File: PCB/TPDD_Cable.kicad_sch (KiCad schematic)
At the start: 9 parts, among them J1 TPDD_RS-232C, P3 RX, P4 RTS, P5 CTS, P6 DSR, Q1 DTA114EKA, Q2 DTA114EKA, Q3 DTA114EKA

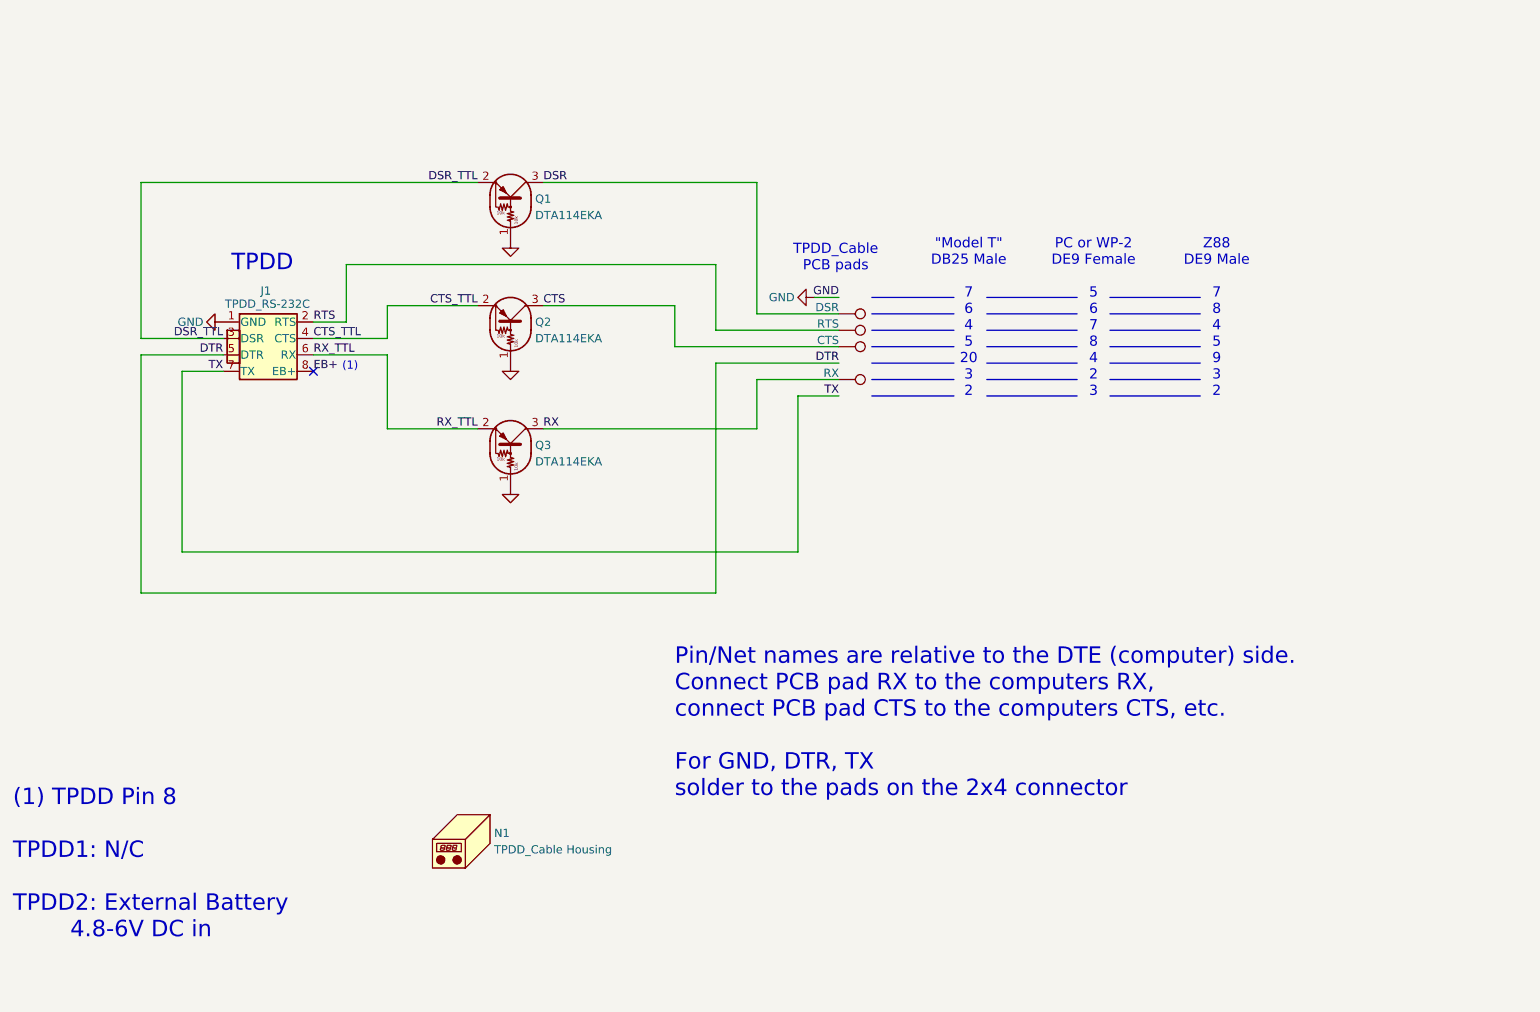
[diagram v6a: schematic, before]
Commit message: schematic less clutter
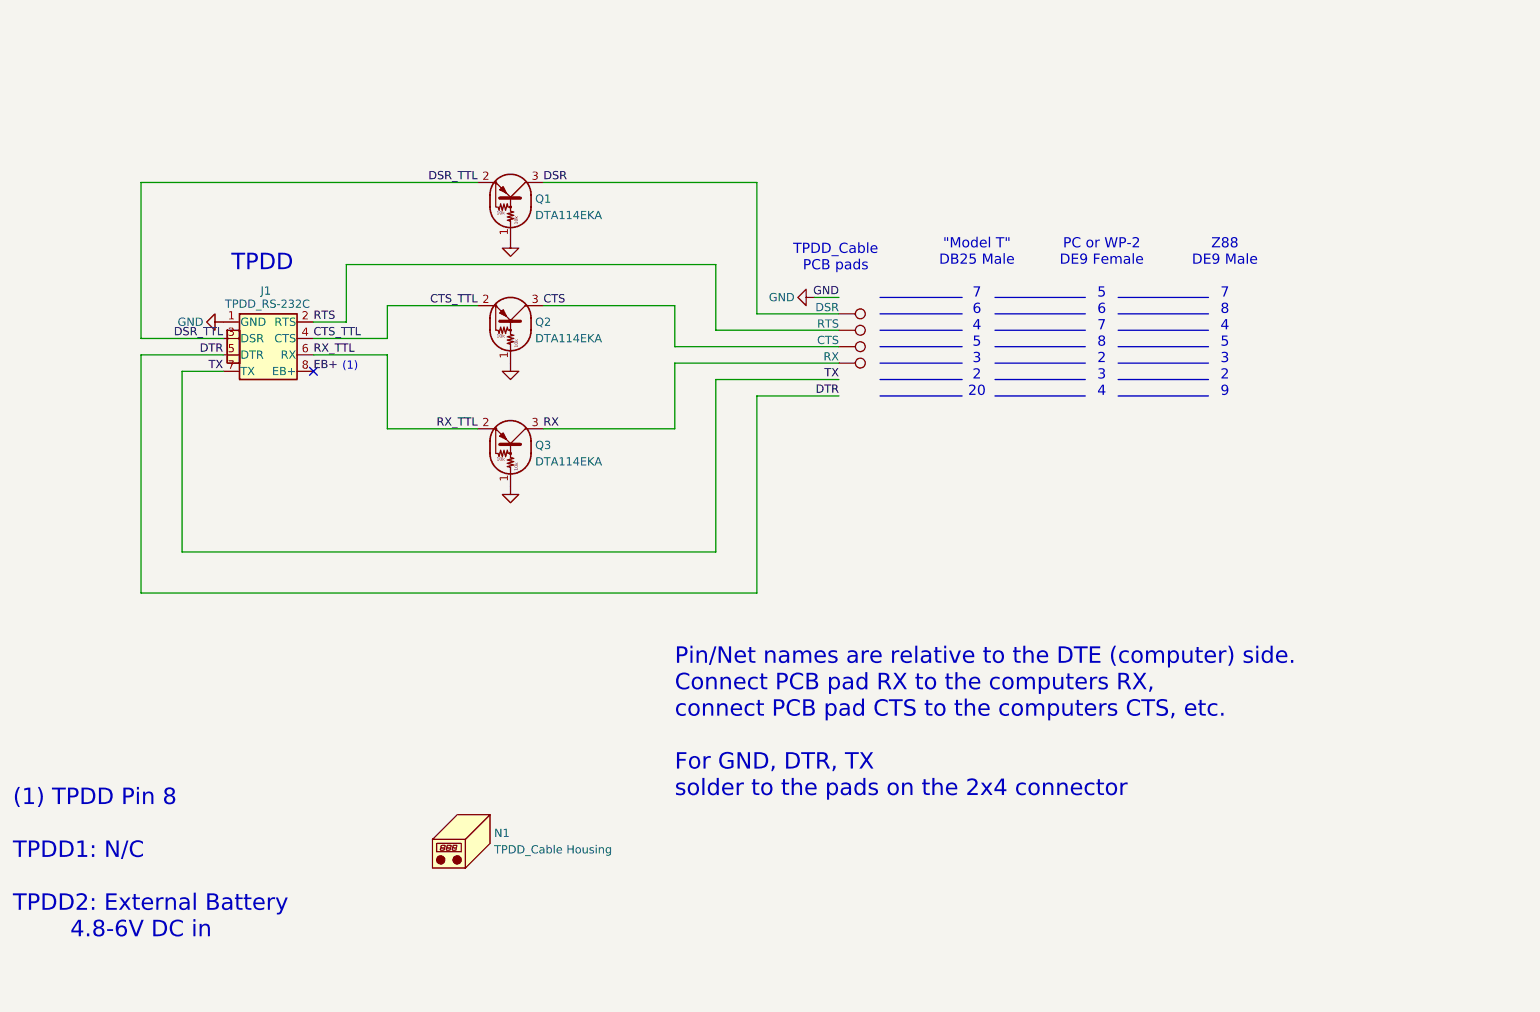
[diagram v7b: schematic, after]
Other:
- note added: ""Model T" DB25 Male 7 6 4 5 3 2 20"
- note added: "PC or WP-2 DE9 Female 5 6 7 8 2 3 4"
- note added: "Z88 DE9 Male 7 8 4 5 3 2 9"
- note removed: ""Model T" DB25 Male 7 6 4 5 20 3 2"
- note removed: "PC or WP-2 DE9 Female 5 6 7 8 4 2 3"
- note removed: "Z88 DE9 Male 7 8 4 5 9 3 2"
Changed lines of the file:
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@@
 	(polyline
 		(pts
-			(xy 194.31 96.52) (xy 208.28 96.52)
-		)
-		(stroke
-			(width 0)
-			(type default)
-		)
-	)
-	(wire
-		(pts
-			(xy 152.4 91.44) (xy 171.45 91.44)
-		)
-		(stroke
-			(width 0)
-			(type default)
-		)
-	)
-	(polyline
-		(pts
-			(xy 194.31 86.36) (xy 208.28 86.36)
-		)
-		(stroke
-			(width 0)
-			(type default)
-		)
-	)
-	(polyline
-		(pts
-			(xy 213.36 88.9) (xy 227.33 88.9)
-		)
-		(stroke
-			(width 0)
-			(type default)
-		)
-	)
-	(polyline
-		(pts
-			(xy 176.53 86.36) (xy 189.23 86.36)
-		)
-		(stroke
-			(width 0)
-			(type default)
-		)
-	)
-	(polyline
-		(pts
-			(xy 213.36 96.52) (xy 227.33 96.52)
+			(xy 195.58 96.52) (xy 209.55 96.52)
+		)
+		(stroke
+			(width 0)
+			(type default)
+		)
+	)
+	(polyline
+		(pts
+			(xy 195.58 86.36) (xy 209.55 86.36)
+		)
+		(stroke
+			(width 0)
+			(type default)
+		)
+	)
+	(polyline
+		(pts
+			(xy 214.63 88.9) (xy 228.6 88.9)
+		)
+		(stroke
+			(width 0)
+			(type default)
+		)
+	)
+	(polyline
+		(pts
+			(xy 177.8 86.36) (xy 190.5 86.36)
+		)
+		(stroke
+			(width 0)
+			(type default)
+		)
+	)
+	(polyline
+		(pts
+			(xy 214.63 96.52) (xy 228.6 96.52)
 		)
 		(stroke
@@
 	(polyline
 		(pts
-			(xy 176.53 93.98) (xy 189.23 93.98)
-		)
-		(stroke
-			(width 0)
-			(type default)
-		)
-	)
-	(wire
-		(pts
-			(xy 165.1 96.52) (xy 171.45 96.52)
-		)
-		(stroke
-			(width 0)
-			(type default)
-		)
-	)
-	(polyline
-		(pts
-			(xy 194.31 81.28) (xy 208.28 81.28)
+			(xy 177.8 93.98) (xy 190.5 93.98)
+		)
+		(stroke
+			(width 0)
+			(type default)
+		)
+	)
+	(wire
+		(pts
+			(xy 152.4 93.98) (xy 171.45 93.98)
+		)
+		(stroke
+			(width 0)
+			(type default)
+		)
+	)
+	(polyline
+		(pts
+			(xy 195.58 81.28) (xy 209.55 81.28)
 		)
 		(stroke
@@
 	(polyline
 		(pts
-			(xy 176.53 88.9) (xy 189.23 88.9)
+			(xy 177.8 88.9) (xy 190.5 88.9)
 		)
 		(stroke
@@
 	(polyline
 		(pts
-			(xy 213.36 86.36) (xy 227.33 86.36)
+			(xy 214.63 86.36) (xy 228.6 86.36)
 		)
 		(stroke
@@
 	(polyline
 		(pts
-			(xy 213.36 91.44) (xy 227.33 91.44)
+			(xy 214.63 91.44) (xy 228.6 91.44)
 		)
 		(stroke
@@
 	(wire
 		(pts
+			(xy 158.75 96.52) (xy 171.45 96.52)
+		)
+		(stroke
+			(width 0)
+			(type default)
+		)
+	)
+	(wire
+		(pts
 			(xy 69.85 92.71) (xy 69.85 120.65)
 		)
@@
 	(polyline
 		(pts
-			(xy 194.31 88.9) (xy 208.28 88.9)
-		)
-		(stroke
-			(width 0)
-			(type default)
-		)
-	)
-	(polyline
-		(pts
-			(xy 213.36 83.82) (xy 227.33 83.82)
-		)
-		(stroke
-			(width 0)
-			(type default)
-		)
-	)
-	(polyline
-		(pts
-			(xy 176.53 81.28) (xy 189.23 81.28)
-		)
-		(stroke
-			(width 0)
-			(type default)
-		)
-	)
-	(wire
-		(pts
-			(xy 63.5 127) (xy 152.4 127)
+			(xy 195.58 88.9) (xy 209.55 88.9)
+		)
+		(stroke
+			(width 0)
+			(type default)
+		)
+	)
+	(polyline
+		(pts
+			(xy 214.63 83.82) (xy 228.6 83.82)
+		)
+		(stroke
+			(width 0)
+			(type default)
+		)
+	)
+	(polyline
+		(pts
+			(xy 177.8 81.28) (xy 190.5 81.28)
+		)
+		(stroke
+			(width 0)
+			(type default)
+		)
+	)
+	(wire
+		(pts
+			(xy 63.5 127) (xy 158.75 127)
 		)
 		(stroke
@@
 	(wire
 		(pts
-			(xy 165.1 96.52) (xy 165.1 120.65)
+			(xy 152.4 93.98) (xy 152.4 120.65)
 		)
 		(stroke
@@
 	(wire
 		(pts
-			(xy 158.75 93.98) (xy 158.75 101.6)
+			(xy 146.05 91.44) (xy 146.05 101.6)
 		)
 		(stroke
@@
 	(wire
 		(pts
-			(xy 125.73 101.6) (xy 158.75 101.6)
+			(xy 125.73 101.6) (xy 146.05 101.6)
 		)
 		(stroke
@@
 	(wire
 		(pts
-			(xy 152.4 91.44) (xy 152.4 127)
+			(xy 158.75 96.52) (xy 158.75 127)
 		)
 		(stroke
@@
 	(polyline
 		(pts
-			(xy 194.31 93.98) (xy 208.28 93.98)
+			(xy 195.58 93.98) (xy 209.55 93.98)
 		)
 		(stroke
@@
 	(polyline
 		(pts
-			(xy 176.53 91.44) (xy 189.23 91.44)
-		)
-		(stroke
-			(width 0)
-			(type default)
-		)
-	)
-	(polyline
-		(pts
-			(xy 176.53 96.52) (xy 189.23 96.52)
+			(xy 177.8 91.44) (xy 190.5 91.44)
+		)
+		(stroke
+			(width 0)
+			(type default)
+		)
+	)
+	(polyline
+		(pts
+			(xy 177.8 96.52) (xy 190.5 96.52)
 		)
 		(stroke
@@
 	(polyline
 		(pts
-			(xy 194.31 91.44) (xy 208.28 91.44)
-		)
-		(stroke
-			(width 0)
-			(type default)
-		)
-	)
-	(polyline
-		(pts
-			(xy 176.53 83.82) (xy 189.23 83.82)
-		)
-		(stroke
-			(width 0)
-			(type default)
-		)
-	)
-	(polyline
-		(pts
-			(xy 213.36 81.28) (xy 227.33 81.28)
-		)
-		(stroke
-			(width 0)
-			(type default)
-		)
-	)
-	(polyline
-		(pts
-			(xy 213.36 93.98) (xy 227.33 93.98)
-		)
-		(stroke
-			(width 0)
-			(type default)
-		)
-	)
-	(wire
-		(pts
-			(xy 158.75 93.98) (xy 171.45 93.98)
+			(xy 195.58 91.44) (xy 209.55 91.44)
+		)
+		(stroke
+			(width 0)
+			(type default)
+		)
+	)
+	(polyline
+		(pts
+			(xy 177.8 83.82) (xy 190.5 83.82)
+		)
+		(stroke
+			(width 0)
+			(type default)
+		)
+	)
+	(polyline
+		(pts
+			(xy 214.63 81.28) (xy 228.6 81.28)
+		)
+		(stroke
+			(width 0)
+			(type default)
+		)
+	)
+	(polyline
+		(pts
+			(xy 214.63 93.98) (xy 228.6 93.98)
+		)
+		(stroke
+			(width 0)
+			(type default)
+		)
+	)
+	(wire
+		(pts
+			(xy 146.05 91.44) (xy 171.45 91.44)
 		)
 		(stroke
@@
 	(polyline
 		(pts
-			(xy 194.31 83.82) (xy 208.28 83.82)
+			(xy 195.58 83.82) (xy 209.55 83.82)
 		)
 		(stroke
@@
 	(wire
 		(pts
-			(xy 69.85 120.65) (xy 165.1 120.65)
+			(xy 69.85 120.65) (xy 152.4 120.65)
 		)
 		(stroke
@@
 		)
 	)
-	(text "Z88\nDE9 Male\n\n7\n8\n4\n5\n9\n3\n2"
-		(exclude_from_sim no)
-		(at 229.87 72.136 0)
+	(text "Z88\nDE9 Male\n\n7\n8\n4\n5\n3\n2\n9"
+		(exclude_from_sim no)
+		(at 231.14 72.136 0)
 		(effects
 			(font
@@
 		)
 	)
-	(text "PC or WP-2\nDE9 Female\n\n5\n6\n7\n8\n4\n2\n3"
-		(exclude_from_sim no)
-		(at 210.82 72.136 0)
+	(text "PC or WP-2\nDE9 Female\n\n5\n6\n7\n8\n2\n3\n4"
+		(exclude_from_sim no)
+		(at 212.09 72.136 0)
 		(effects
 			(font
@@
 		)
 	)
-	(text "\"Model T\"\nDB25 Male\n\n7\n6\n4\n5\n20\n3\n2"
-		(exclude_from_sim no)
-		(at 191.516 72.136 0)
+	(text "\"Model T\"\nDB25 Male\n\n7\n6\n4\n5\n3\n2\n20"
+		(exclude_from_sim no)
+		(at 192.786 72.136 0)
 		(effects
 			(font
@@
 	)
 	(label "DTR"
-		(at 171.45 91.44 180)
+		(at 171.45 96.52 180)
 		(fields_autoplaced yes)
 		(effects
@@
 	)
 	(label "TX"
-		(at 171.45 96.52 180)
+		(at 171.45 93.98 180)
 		(fields_autoplaced yes)
 		(effects
@@
 	(symbol
 		(lib_id "000_LOCAL:TestPoint")
-		(at 171.45 93.98 270)
+		(at 171.45 91.44 270)
 		(unit 1)
 		(exclude_from_sim no)
@@
 		(dnp no)
 		(property "Reference" "P3"
-			(at 175.514 92.964 90)
+			(at 175.514 90.424 90)
 			(effects
 				(font
@@
 		)
 		(property "Value" "RX"
-			(at 171.45 93.726 90)
+			(at 171.45 91.186 90)
 			(effects
 				(font
@@
 		)
 		(property "Footprint" "000_LOCAL:SMD_1.2x3"
-			(at 171.45 99.06 0)
+			(at 171.45 96.52 0)
 			(effects
 				(font
@@
 		)
 		(property "Datasheet" "~"
-			(at 171.45 99.06 0)
+			(at 171.45 96.52 0)
 			(effects
 				(font
@@
 		)
 		(property "Description" "test point"
-			(at 171.45 93.98 0)
-			(effects
-				(font
+			(at 171.45 91.44 0)
+			(effects
+				(font
